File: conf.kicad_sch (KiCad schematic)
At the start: 56 parts, among them Q401 DNLS350E, Q402 DNLS350E, Q403 DPLS350E, Q404 DPLS350E, U401 SN74LVC1G04DBVR, U402 4085, U403 AD567xR, U404 TLV9352, U405 4041

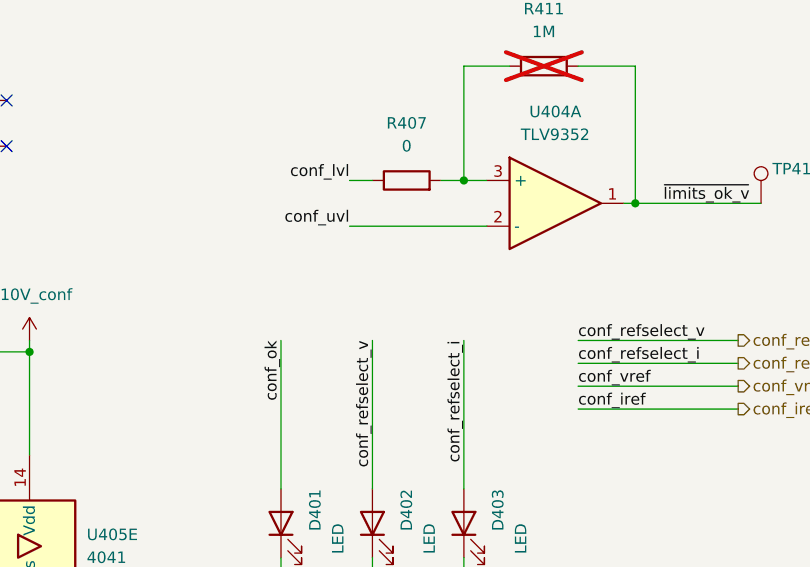
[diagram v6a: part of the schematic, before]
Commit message: add pss lightpipe to schematic
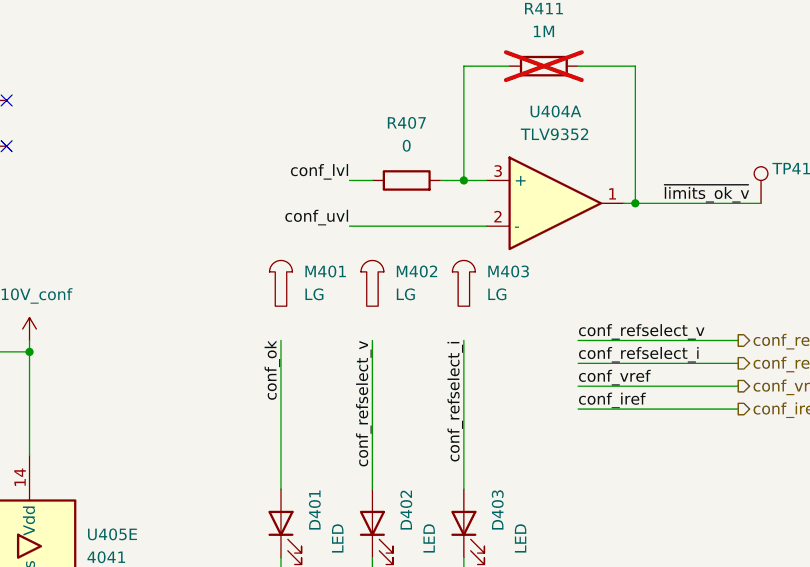
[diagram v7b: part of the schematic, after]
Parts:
- added M401, M402, M403: LG, symbol pss:Lightguide_D4mm_L22.86mm_Dout5mm

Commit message: fix pss lightpipe length variant selection
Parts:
- M401, M402, M403: MPN 51513510900F -> 51513510188F; VPN 645-51513510900F -> 645-51513510188F
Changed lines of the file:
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@@
 			)
 		)
-		(property "MPN" "51513510900F"
+		(property "MPN" "51513510188F"
 			(at 165.1 149.86 0)
 			(effects
@@
 			)
 		)
-		(property "VPN" "645-51513510900F"
+		(property "VPN" "645-51513510188F"
 			(at 165.1 149.86 0)
 			(effects
@@
 			)
 		)
-		(property "MPN" "51513510900F"
+		(property "MPN" "51513510188F"
 			(at 144.78 149.86 0)
 			(effects
@@
 			)
 		)
-		(property "VPN" "645-51513510900F"
+		(property "VPN" "645-51513510188F"
 			(at 144.78 149.86 0)
 			(effects
@@
 			)
 		)
-		(property "MPN" "51513510900F"
+		(property "MPN" "51513510188F"
 			(at 154.94 149.86 0)
 			(effects
@@
 			)
 		)
-		(property "VPN" "645-51513510900F"
+		(property "VPN" "645-51513510188F"
 			(at 154.94 149.86 0)
 			(effects
